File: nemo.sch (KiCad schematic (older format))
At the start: 20 parts, among them J1 Conn_01x02_Male, J2 Conn_01x06_Male, J3 Conn_01x02_Male, J4 Conn_01x06_Male, J5 Conn_02x03_Odd_Even, J6 Conn_01x12_Male, SW1 SW_Push, U1 ATmega328P-AU, U2 L7805, Y1 16MHz

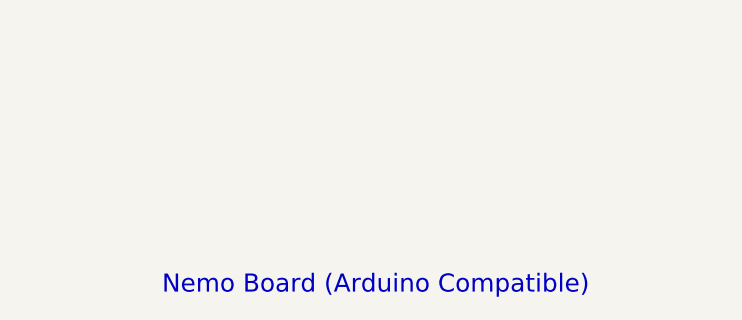
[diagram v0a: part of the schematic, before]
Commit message: * Added README.md * Added BOM - bom.csv * Exportet schematic to pdf - schematic.pdf
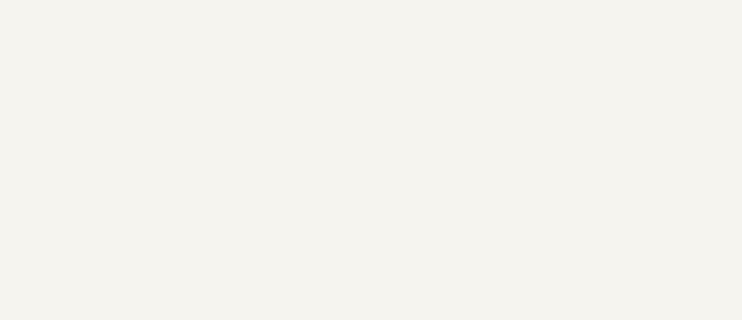
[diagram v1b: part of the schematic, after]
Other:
- note removed: "Nemo Board (Arduino Compatible)"
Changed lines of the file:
@@
 encoding utf-8
 Sheet 1 1
-Title ""
-Date ""
-Rev ""
-Comp ""
+Title "Nemo Board (Arduino Compatible)"
+Date "2020-05-23"
+Rev "1"
+Comp "Patric A.B"
 Comment1 ""
 Comment2 ""
@@
 	1    0    0    -1
 $EndComp
-Text Notes 7400 7500 0    79   ~ 0
-Nemo Board (Arduino Compatible)
 Wire Wire Line
 	3450 1150 3650 1150
